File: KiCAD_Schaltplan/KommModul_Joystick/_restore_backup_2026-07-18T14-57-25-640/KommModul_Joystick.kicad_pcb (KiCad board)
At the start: 2 copper layers, 100 x 100 mm, 65 parts, among them J1 66100411622, J2 618015231121, J3 691242510004, J4 691242510004, J5 612020235121, J6 696106003002, SW1 430182080816, SW3 472123010111, U1 STM32F303RETx, U2 SP3485EN, U3 SP3485EN, U4 TLV1117LV33DCYR, Y1 16 MHz

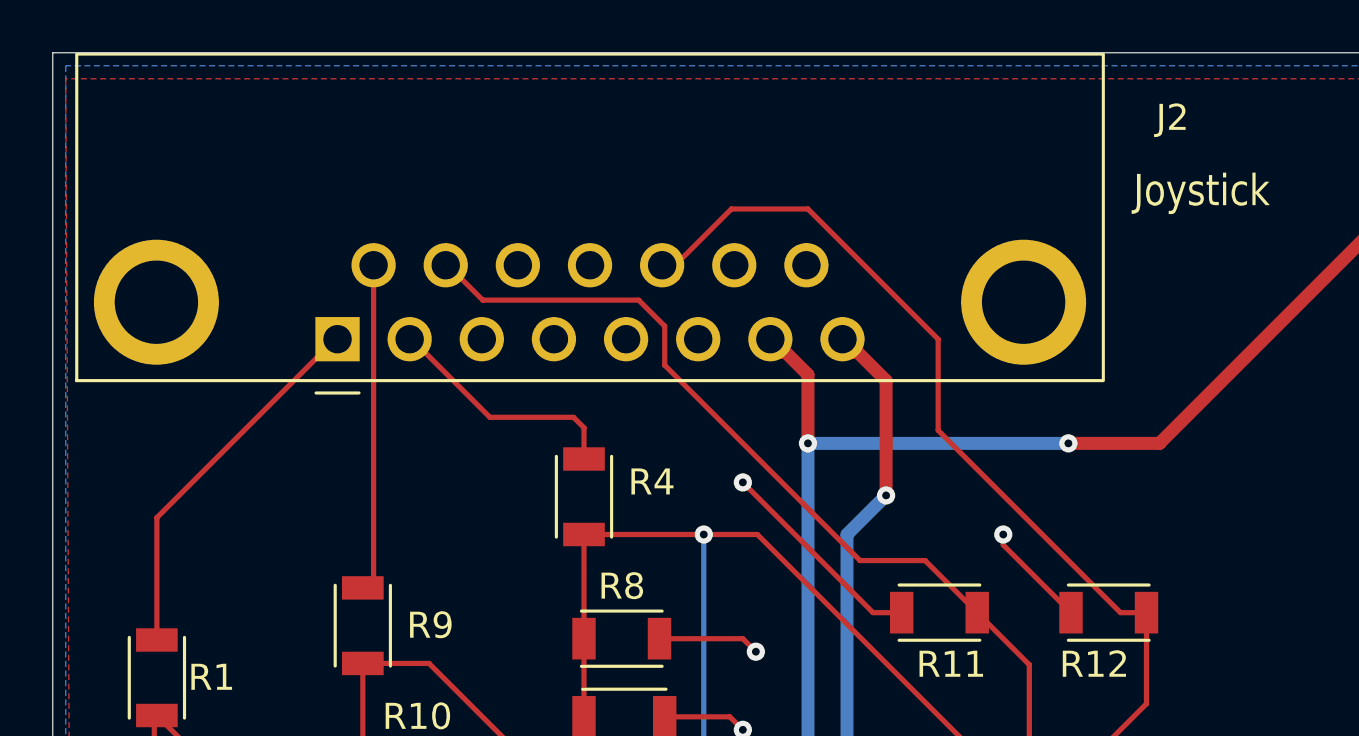
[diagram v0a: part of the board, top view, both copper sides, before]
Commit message: J2 to the edge of PCB
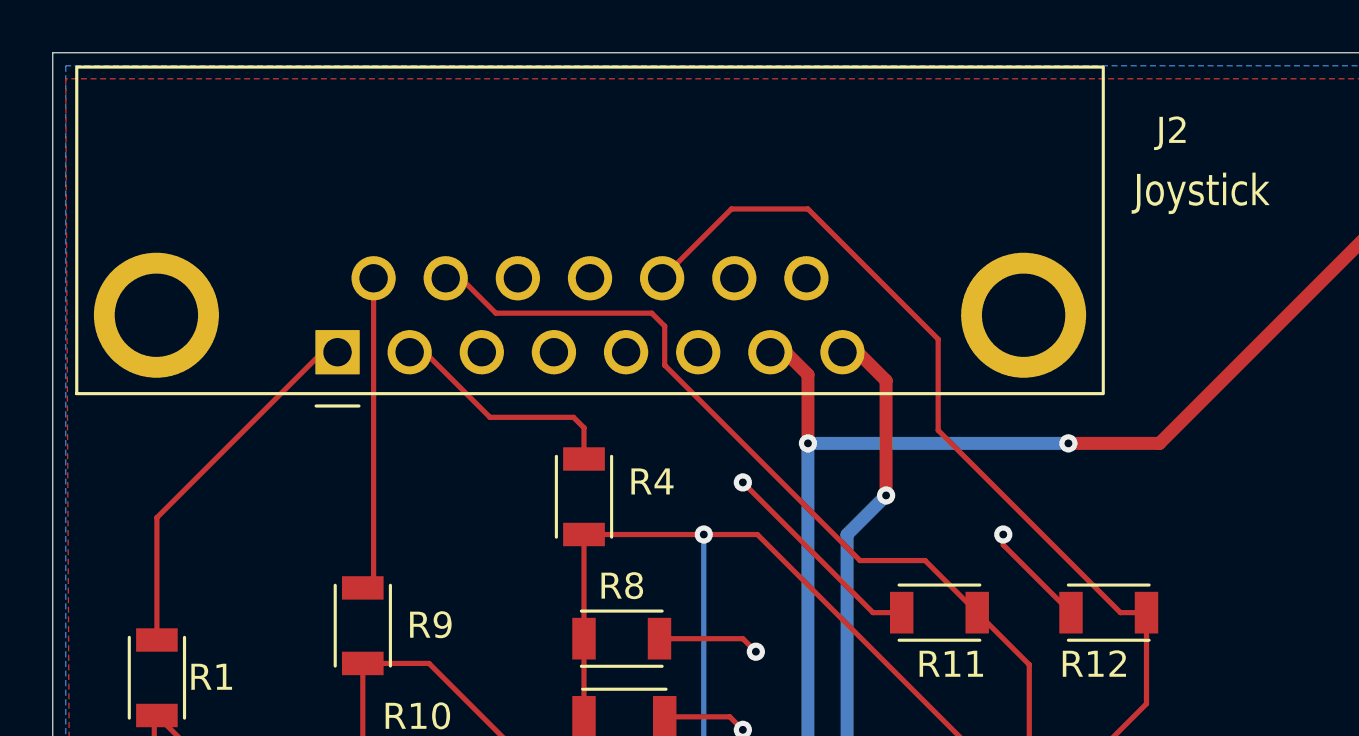
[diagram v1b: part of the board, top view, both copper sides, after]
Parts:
- moved J2 0.50 mm to (90.9, 46.5)
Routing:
- net Net-(J2-Pad9): track 12.6 -> 12.1 mm
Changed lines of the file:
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@@
 		)
 		(pad_to_mask_clearance 0)
+		(solder_mask_min_width 0.1)
 		(allow_soldermask_bridges_in_footprints no)
 		(tenting
@@
 	(footprint "Library:J_Wurth_WR-DSUB_618015231121"
 		(layer "F.Cu")
-		(at 90.936038 46 90)
+		(at 90.936038 46.5 90)
 		(descr "8.08 mm Female Angled PCB Connector w. Hex Screw, body 39.2x18.4x16.55mm, https://www.we-online.com/en/components/products/datasheet/618015231121?ki")
 		(tags "THT")
@@
 	)
 	(segment
-		(start 110.909614 46.5)
-		(end 110.826038 46.5)
-		(width 0.5)
-		(layer "F.Cu")
-		(net "/VCC_3_3V")
-	)
-	(segment
-		(start 112 52)
-		(end 112 47.590386)
-		(width 0.5)
-		(layer "F.Cu")
-		(net "/VCC_3_3V")
-	)
-	(segment
 		(start 126.25 71.70312)
 		(end 126.25 70.825)
@@
 	)
 	(segment
+		(start 110.909614 46.5)
+		(end 110.326038 46.5)
+		(width 0.5)
+		(layer "F.Cu")
+		(net "/VCC_3_3V")
+	)
+	(segment
 		(start 126.25 69.5)
 		(end 126.25 68.75)
@@
 	)
 	(segment
+		(start 112 47.590386)
+		(end 110.909614 46.5)
+		(width 0.5)
+		(layer "F.Cu")
+		(net "/VCC_3_3V")
+	)
+	(segment
 		(start 137 101)
 		(end 140 104)
@@
 	)
 	(segment
-		(start 110.826038 46.5)
-		(end 110.326038 46)
-		(width 0.5)
-		(layer "F.Cu")
-		(net "/VCC_3_3V")
-	)
-	(segment
 		(start 147 94)
 		(end 147 88)
@@
 	)
 	(segment
+		(start 112 52)
+		(end 112 47.590386)
+		(width 0.5)
+		(layer "F.Cu")
+		(net "/VCC_3_3V")
+	)
+	(segment
 		(start 140.5 103)
 		(end 143 103)
@@
 	)
 	(segment
-		(start 112 47.590386)
-		(end 110.909614 46.5)
-		(width 0.5)
-		(layer "F.Cu")
-		(net "/VCC_3_3V")
-	)
-	(segment
 		(start 141.5 106.5)
 		(end 141 106.5)
@@
 	)
 	(segment
-		(start 105.5 82)
-		(end 105 81.5)
+		(start 109 47.360386)
+		(end 108.139614 46.5)
 		(width 0.5)
 		(layer "F.Cu")
@@
 	)
 	(segment
-		(start 108.056038 46.5)
-		(end 107.556038 46)
+		(start 105.5 82)
+		(end 105 81.5)
 		(width 0.5)
 		(layer "F.Cu")
@@
 	)
 	(segment
-		(start 105.55 89)
-		(end 105.5 88.95)
+		(start 108.139614 46.5)
+		(end 107.556038 46.5)
 		(width 0.5)
 		(layer "F.Cu")
@@
 	)
 	(segment
-		(start 108.139614 46.5)
-		(end 108.056038 46.5)
+		(start 105.55 89)
+		(end 105.5 88.95)
 		(width 0.5)
 		(layer "F.Cu")
@@
 	)
 	(segment
-		(start 131.2 103.3)
-		(end 128.035688 103.3)
+		(start 109 50)
+		(end 109 47.360386)
 		(width 0.5)
 		(layer "F.Cu")
@@
 	)
 	(segment
-		(start 109 50)
-		(end 109 47.360386)
+		(start 131.2 103.3)
+		(end 128.035688 103.3)
 		(width 0.5)
 		(layer "F.Cu")
@@
 	)
 	(segment
-		(start 109 47.360386)
-		(end 108.139614 46.5)
-		(width 0.5)
-		(layer "F.Cu")
-		(net "/VCC_5V")
-	)
-	(segment
 		(start 108 89)
 		(end 105.55 89)
@@
 	)
 	(segment
-		(start 121 56.5)
-		(end 122 56.5)
-		(width 0.2)
-		(layer "F.Cu")
-		(net "/JS_Taster1")
-	)
-	(segment
-		(start 117.099997 64.5)
-		(end 117.5 64.5)
+		(start 114 46)
+		(end 114 49.5)
 		(width 0.2)
 		(layer "F.Cu")
@@
 	)
 	(segment
-		(start 117 64.599997)
-		(end 117.099997 64.5)
+		(start 114 49.5)
+		(end 121 56.5)
 		(width 0.2)
 		(layer "F.Cu")
@@
 	)
 	(segment
-		(start 114 49.5)
-		(end 121 56.5)
-		(width 0.2)
-		(layer "F.Cu")
-		(net "/JS_Taster1")
-	)
-	(segment
-		(start 139.349997 79.75)
-		(end 135.675 79.75)
+		(start 117.099997 64.5)
+		(end 117.5 64.5)
 		(width 0.2)
 		(layer "F.Cu")
@@
 	)
 	(segment
-		(start 139.5 79.599997)
-		(end 139.349997 79.75)
+		(start 117 64.599997)
+		(end 117.099997 64.5)
 		(width 0.2)
 		(layer "F.Cu")
@@
 	)
 	(segment
-		(start 103.401038 43.16)
-		(end 103.901038 43.66)
+		(start 103.401038 43.66)
+		(end 103.984614 43.66)
 		(width 0.2)
 		(layer "F.Cu")
@@
 	)
 	(segment
-		(start 103.401038 43.16)
-		(end 103.901038 43.16)
+		(start 139.349997 79.75)
+		(end 135.675 79.75)
 		(width 0.2)
 		(layer "F.Cu")
@@
 	)
 	(segment
-		(start 114 46)
-		(end 114 49.5)
+		(start 139.5 79.599997)
+		(end 139.349997 79.75)
 		(width 0.2)
 		(layer "F.Cu")
@@
 	)
 	(segment
-		(start 117.5 64.5)
-		(end 122 60)
+		(start 106.061038 41)
+		(end 109 41)
 		(width 0.2)
 		(layer "F.Cu")
@@
 	)
 	(segment
-		(start 106.061038 41)
-		(end 109 41)
+		(start 103.401038 43.66)
+		(end 106.061038 41)
 		(width 0.2)
 		(layer "F.Cu")
@@
 	)
 	(segment
-		(start 103.901038 43.16)
-		(end 106.061038 41)
+		(start 121 56.5)
+		(end 122 56.5)
 		(width 0.2)
 		(layer "F.Cu")
@@
 	)
 	(segment
-		(start 103.901038 43.66)
-		(end 103.984614 43.66)
+		(start 117.5 64.5)
+		(end 122 60)
 		(width 0.2)
 		(layer "F.Cu")
@@
 	)
 	(segment
-		(start 93.706038 46)
-		(end 94.206038 46.5)
-		(width 0.2)
-		(layer "F.Cu")
-		(net "Net-(J2-Pad2)")
-	)
-	(segment
 		(start 100.4 49.4)
 		(end 100.4 50.6)
@@
 	)
 	(segment
-		(start 96.789614 49)
-		(end 100 49)
+		(start 93.706038 46.5)
+		(end 94.289614 46.5)
 		(width 0.2)
 		(layer "F.Cu")
@@
 	)
 	(segment
-		(start 94.206038 46.5)
-		(end 94.289614 46.5)
+		(start 94.289614 46.5)
+		(end 96.789614 49)
 		(width 0.2)
 		(layer "F.Cu")
@@
 	)
 	(segment
-		(start 94.289614 46.5)
-		(end 96.789614 49)
+		(start 96.789614 49)
+		(end 100 49)
 		(width 0.2)
 		(layer "F.Cu")
@@
 	)
 	(segment
-		(start 103.5 47)
-		(end 111 54.5)
+		(start 139.5 76.899988)
+		(end 139.100012 76.899988)
 		(width 0.2)
 		(layer "F.Cu")
@@
 	)
 	(segment
-		(start 113.5 54.5)
-		(end 115.5 56.5)
+		(start 103.5 45.5)
+		(end 103.5 47)
 		(width 0.2)
 		(layer "F.Cu")
@@
 	)
 	(segment
-		(start 96.514614 44.5)
-		(end 102.5 44.5)
+		(start 95.091038 43.66)
+		(end 95.674614 43.66)
 		(width 0.2)
 		(layer "F.Cu")
@@
 	)
 	(segment
-		(start 139.5 76.899988)
-		(end 139.100012 76.899988)
+		(start 117.5 58.5)
+		(end 115.5 56.5)
 		(width 0.2)
 		(layer "F.Cu")
@@
 	)
 	(segment
-		(start 103.5 45.5)
-		(end 103.5 47)
+		(start 103.5 47)
+		(end 111 54.5)
 		(width 0.2)
 		(layer "F.Cu")
@@
 	)
 	(segment
-		(start 117.5 58.5)
-		(end 115.5 56.5)
+		(start 95.674614 43.66)
+		(end 97.014614 45)
 		(width 0.2)
 		(layer "F.Cu")
@@
 	)
 	(segment
-		(start 102.5 44.5)
-		(end 103.5 45.5)
+		(start 113.5 54.5)
+		(end 115.5 56.5)
 		(width 0.2)
 		(layer "F.Cu")
@@
 	)
 	(segment
-		(start 95.591038 43.66)
-		(end 95.674614 43.66)
+		(start 103 45)
+		(end 103.5 45.5)
 		(width 0.2)
 		(layer "F.Cu")
@@
 	)
 	(segment
-		(start 111 54.5)
-		(end 113.5 54.5)
+		(start 97.014614 45)
+		(end 103 45)
 		(width 0.2)
 		(layer "F.Cu")
@@
 	)
 	(segment
-		(start 95.091038 43.16)
-		(end 95.591038 43.66)
+		(start 111 54.5)
+		(end 113.5 54.5)
 		(width 0.2)
 		(layer "F.Cu")
@@
 	)
 	(segment
-		(start 95.674614 43.66)
-		(end 96.514614 44.5)
-		(width 0.2)
-		(layer "F.Cu")
-		(net "/JS_Taster2")
-	)
-	(segment
 		(start 137.75 78.25)
 		(end 135.675 78.25)
@@
 	)
 	(segment
-		(start 92.321038 55.135346)
-		(end 91.906384 55.55)
+		(start 92.321038 43.66)
+		(end 92.321038 55.135346)
 		(width 0.2)
 		(layer "F.Cu")
@@
 	)
 	(segment
-		(start 92.321038 43.16)
-		(end 92.321038 55.135346)
+		(start 92.321038 55.135346)
+		(end 91.906384 55.55)
 		(width 0.2)
 		(layer "F.Cu")
@@
 	)
 	(segment
-		(start 83.9 57.45)
-		(end 84 57.55)
+		(start 84 57.55)
+		(end 84 52.852462)
 		(width 0.2)
 		(layer "F.Cu")
@@
 	(segment
 		(start 90.352462 46.5)
-		(end 90.436038 46.5)
-		(width 0.2)
-		(layer "F.Cu")
-		(net "Net-(J2-Pad1)")
-	)
-	(segment
-		(start 84 52.852462)
-		(end 90.352462 46.5)
+		(end 90.936038 46.5)
 		(width 0.2)
 		(layer "F.Cu")
@@
 	)
 	(segment
-		(start 90.436038 46.5)
-		(end 90.936038 46)
+		(start 83.9 57.45)
+		(end 84 57.55)
 		(width 0.2)
 		(layer "F.Cu")
@@
 	)
 	(segment
-		(start 84 57.55)
-		(end 84 52.852462)
+		(start 84 52.852462)
+		(end 90.352462 46.5)
 		(width 0.2)
 		(layer "F.Cu")
